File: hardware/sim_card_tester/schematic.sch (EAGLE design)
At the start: 146 parts, among them IC1 TPS6300, J2 MICRO_USB_B_HIROSE_ZX62R-B-5P, J3 CON_MICRO_SDDM3AT-SF-PEJM5, J4 NANO_SIM, J5 NANO_SIM, J6 TC2030-JLINK-NL, J7 NANO_SIM, J8 NANO_SIM, J9 U.FL-R-SMT, Q11 SI223DDS, Q3 MOSFET-NCHANNELSMD, Q4 MOSFET-NCHANNELSMD, Q5 MOSFET-NCHANNELSMD, U1 AB1815-T3, U10 SIP32510, U11 SIP32510, U14 SARA-U2, U15 MAX4734EUB+, U16 SARA-U2, U17 TXB0104RUT, U2 BGA725L6-ALT, U20 MAX4734EUB+, U21 MAX4734EUB+, U22 MAX4734EUB+, U3 FTDI234XD, U4 SAFFB1G56KB0F0A, U5 MAX8887EZK33+T, U6 MCP73831, U7 MAX-M8, U8 MAX67XXMAX6749MAX67XX, U9 NRF52840, X1 ABS07-32.768KHZ-7-T, X4 32MHz, X5 32.768kHz

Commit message: second pcb
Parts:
- removed C13: 33pF, passives:CAPACITOR0603_CAP
- removed C15: 100uF, passives:CAPACITOR0805_CAP
- removed C22, C24, C25, C26: 47pF, passives:CAPACITOR0402_CAP
- removed C49: 56pF, passives:CAPACITOR0402_CAP
- removed C50: 10nF, passives:CAPACITOR0402_CAP
- removed C51: 100nF, passives:CAPACITOR0402_CAP
- removed C52: 220uF, passives:CAPACITOR1210_CAP
- removed D10, D11, D8, D9: 14V, passives:DIODE_ZENER0402
- removed J9: U.FL-R-SMT, connector:U.FL-R-SMT
- removed Q11: SI223DDS, fets:SI223DDS
- removed Q4, Q5: MOSFET-NCHANNELSMD, fets:MOSFET-NCHANNELSMD
- removed R25: 10k, passives:RESISTOR0402_RES
- removed R36: 0, passives:RESISTOR0402_RES
- removed R40, R42: 100k, passives:RESISTOR0402_RES
- removed R45: 100, passives:RESISTOR0402_RES
- removed U14, U16: SARA-U2, ubloxLib:SARA-U2
- removed U17: TXB0104RUT, chips:TXB0104RUT
- added C11, C12, C16, C28: 47pF, passives:CAPACITOR0402_CAP
- added C17: 56pF, passives:CAPACITOR0402_CAP
- added C18: 100uF, passives:CAPACITOR0805_CAP
- added C19: 10nF, passives:CAPACITOR0402_CAP
- added C20: 220uF, passives:CAPACITOR1210_CAP
- added C21: 100nF, passives:CAPACITOR0402_CAP
- added C27: 33pF, passives:CAPACITOR0603_CAP
- added D3, D4, D6, D7: 14V, passives:DIODE_ZENER0402
- added J13: U.FL-R-SMT, connector:U.FL-R-SMT
- added Q2, Q6: MOSFET-NCHANNELSMD, fets:MOSFET-NCHANNELSMD
- added Q7: SI223DDS, fets:SI223DDS
- added R10: 10k, passives:RESISTOR0402_RES
- added R43, R46: 100k, passives:RESISTOR0402_RES
- added R47: 0, passives:RESISTOR0402_RES
- added R48: 100, passives:RESISTOR0402_RES
- added U12: UBLOX_SARA_G350, signpost:UBLOX_SARA_G350
- added U13: TXB0104RUT, chips:TXB0104RUT
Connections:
- removed net N$10: C13.2, R36.2
- removed net N$11: C13.1, U16A.ANT
- removed net N$50: J9.ANT, R36.1
- removed net N$52: Q4.D, Q5.D, U16A.DTR
- removed net N$54: Q4.S, U16A.!RESET
- removed net N$56: R42.2
- removed net N$57: Q5.S, U16A.PWR_ON
- removed net N$58: U16A.RTS, U17.A1
- removed net N$62: U16A.CTS, U17.A2
- removed net N$7: R25.1, U17.OE
- removed net N$80: Q11.G, R45.1
- removed net N$95: C22.2, C24.2, C25.2, C26.2, D10.ANODE, D11.ANODE, D8.ANODE, D9.ANODE
- removed net RXD: U16A.RXD, U17.A4
- removed net TXD: U16A.TXD, U17.A3
- removed net VBCKP: C15.1, R42.1, U14B.V_BCKP
- new net 3V3: R10.2, U13.VCC_B
- new net N$12: U12.RXD, U13.A4
- new net N$15: Q6.D, U12.RESET_N
- new net N$16: C18.1, R43.2, U12.V_BCKP
- new net N$18: Q2.D, R43.1, U12.PWR_ON
- new net N$25: U12.CTS, U13.A2
- new net N$53: U12.RTS, U13.A1
- new net N$63: C27.2, R47.1
- new net N$66: Q7.G, R48.1
- new net N$68: R10.1, U13.OE
- new net N$69: C27.1, U12.ANT
- new net N$70: J13.ANT, R47.2
- new net N$71: C11.2, C12.2, C16.2, C28.2, D3.ANODE, D4.ANODE, D6.ANODE, D7.ANODE
- new net N$9: U12.TXD, U13.A3
- net +3V3: no longer R25.2, U17.VCC_B
- net CLK_SIM: now also C28.1, D7.CATHODE, U12.SIM_CLK; no longer C26.1, D11.CATHODE, U14B.SIM_CLK
- net GND: now also C17.2, C18.2, C19.2, C20.2, C21.2, J13.P$2, Q2.S, Q6.S, R46.1, U12.DTR, U12.GND, U13.GND; no longer C15.2, C49.2, C50.2, C51.2, C52.2, J9.P$2, R40.1, U17.GND
- net GSM_3V8: now also Q7.S; no longer Q11.S
- net GSM_CTS: now also U13.B1; no longer U17.B1
- net GSM_GATED: now also C17.1, C19.1, C20.1, C21.1, Q7.D, U12.VCC; no longer C49.1, C50.1, C51.1, C52.1, Q11.D, U14B.VCC@3
- net GSM_LED: now also U12.GPIO1; no longer U16A.GPIO1
- net GSM_POWER: now also Q2.G; no longer Q5.G
- net GSM_POWER_GATE: now also R46.2, R48.2; no longer R40.2, R45.2
- net GSM_RST: now also Q6.G; no longer Q4.G
- net GSM_RTS: now also U13.B2; no longer U17.B2
- net GSM_RX: now also U13.B3; no longer U17.B3
- net GSM_TX: now also U13.B4; no longer U17.B4
- net IO_SIM: now also C11.1, D4.CATHODE, U12.SIM_IO; no longer C22.1, D9.CATHODE, U14B.SIM_IO
- net RST_SIM: now also C12.1, D6.CATHODE, U12.SIM_RST; no longer C24.1, D10.CATHODE, U14B.SIM_RST
- net VCC_SIM: now also C16.1, D3.CATHODE, U12.VSIM; no longer C25.1, D8.CATHODE, U14B.VSIM
- net V_GSM_INT: now also U12.V_INT, U13.VCC_A; no longer U14B.V_INT, U17.VCC_A
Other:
- note added: "UART lines for commands"

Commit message: fixed schematic and nrf routing
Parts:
- removed 20UF: (no value), Nordic_nRF:CAPACITOR_0201_L
- removed A4: ANT3216A063R2400A, chips:ANT3216A063R2400A
- removed C39: 1pF, passives:CAPACITOR0402_CAP
- removed L8: 3.9nH, passives:INDUCTOR0402
- removed LED1: BLUE, leds:LED0603
- removed Q3: MOSFET-NCHANNELSMD, fets:MOSFET-NCHANNELSMD
- removed R14: 10k, passives:RESISTOR0402_RES
- removed R20: 1k, passives:RESISTOR0402_RES
- removed R21: 100k, passives:RESISTOR0402_RES
- removed R47: 0, passives:RESISTOR0402_RES
- removed TP4: TPTP06SQ, testpad:TPTP06SQ
- added C50: 10uF, Nordic_nRF:CAPACITOR_0603_L
- added LED2: BLUE, leds:LED0603
- added Q1: MOSFET-NCHANNELSMD, fets:MOSFET-NCHANNELSMD
- added R11: 1k, BeagleBone_Black_Wireless:R-US_R0603
- added R12: 100k, BeagleBone_Black_Wireless:R-US_R0603
- 10UF: value (none) -> 10uF; device Nordic_nRF:CAPACITOR_0201_L -> Nordic_nRF:CAPACITOR_0603_L
- C11, C12, C14, C16, C17, C19, C2, C21, C23, C28, C3, C30, C31, C32, C33, C34, C35, C36, C37, C38, C4, C41, C42, C43, C44, C5, C55, C56, C58, C59, C6, C60, C61, C67, C68, C7, C8, C9: device passives:CAPACITOR0402_CAP -> Nordic_nRF:CAPACITOR_0603_L
- C18: device passives:CAPACITOR0805_CAP -> Nordic_nRF:CAPACITOR_0603_L
- C20: device passives:CAPACITOR1210_CAP -> Nordic_nRF:CAPACITOR_0603_L
- C27: device passives:CAPACITOR0603_CAP -> Nordic_nRF:CAPACITOR_0603_L
- C40: value 1pF -> 10uF; device passives:CAPACITOR0402_CAP -> Nordic_nRF:CAPACITOR_0603_L; DIGIKEY 490-3083-1-ND -> (none); MPN GJM1555C1H1R0CB01D -> (none)
- R1, R10, R13, R15, R16, R17, R18, R19, R2, R22, R27, R29, R3, R30, R31, R32, R33, R34, R35, R4, R41, R43, R46, R48, R5, R6, R7, R8, R9: device passives:RESISTOR0402_RES -> BeagleBone_Black_Wireless:R-US_R0603
- R23: device SparkFun-Resistors:100OHM-0603-1/4W-5% -> BeagleBone_Black_Wireless:R-US_R0603
- R24, R37, R38, R39: device SparkFun-Resistors:10KOHM-0603-1/10W-1% -> BeagleBone_Black_Wireless:R-US_R0603
- R26, R28: device SparkFun-Resistors:RESISTOR0402 -> BeagleBone_Black_Wireless:R-US_R0603
- U$5: device Nordic_nRF:CAPACITOR_0201_L -> Nordic_nRF:CAPACITOR_0603_L
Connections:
- removed net 0: J4.C5(GND), J5.C5(GND), J7.C5(GND), J8.C5(GND), U15.GND, U20.GND, U21.GND, U22.GND
- removed net 3V3: R10.2, U13.VCC_B
- removed net 5V: C67.1, FB2.P$2, J2.+5V, R41.1, R8.2, U6.VDD/1, U6.VDD/2
- removed net CONNECT: 10UF.1, C68.1, IC1G$1.VIN, R13.2, R23.2, U6.VBAT/3, U6.VBAT/4
- removed net GSM_3V8: Q7.S
- removed net N$30: IC1G$1.PGND
- removed net N$37: IC1G$1.GND
- removed net N$38: C39.1, L8.2, U9.ANT
- removed net N$42: A4.ANTENNA, C40.1, L8.1
- removed net N$44: LED1.CATHODE, Q3.D
- removed net N$49: LED1.ANODE, R20.1
- removed net N$51: 20UF.1, C58.1, IC1G$1.VOUT, R26.2, U5.!SHDN, U5.IN
- removed net N$63: C27.2, R47.1
- removed net RTC_CS: U9.P0.12
- removed net RTC_INT1: U9.P0.16
- new net N$14: LED2.CATHODE, Q1.D
- new net N$23: LED2.ANODE, R11.1
- net !EXTERNAL_RST: now also U9.P0.24
- net !RTC_CS: now also U9.P0.12
- net !RTC_INT1: now also U9.P0.16
- net +3V3: now also C10.1, C40.1, C50.1, C58.1, C67.1, IC1G$1.VOUT, Q7.S, R10.2, R15.1, R16.1, R26.2, R41.1, R8.2, U1.VCC, U13.VCC_B, U5.!SHDN, U5.IN, U6.VDD/1, U6.VDD/2
- net BAT: now also 10UF.1, C68.1, IC1G$1.VIN, R13.2, R23.2, U6.VBAT/3, U6.VBAT/4
- net BATIN: now also U9.P1.06; no longer U9.P0.30/AIN6
- net GND: now also C50.2, IC1G$1.GND, IC1G$1.PGND, J4.C5(GND), J5.C5(GND), J7.C5(GND), J8.C5(GND), Q1.S, R12.1, U15.GND, U20.GND, U21.GND, U22.GND; no longer 20UF.2, A4.GND, C39.2, Q3.S, R14.2, R21.1, TP4.TP
- net GSM_CTS: now also U9.P0.02/AIN0
- net GSM_GATED: now also R11.2; no longer R20.2
- net GSM_LED: now also Q1.G, R12.2; no longer Q3.G, R21.2
- net GSM_POWER: now also U9.P0.03/AIN1
- net GSM_RST: now also U9.P0.29/AIN5
- net GSM_RTS: now also U9.P0.28/AIN4
- net GSM_RX: now also U9.P0.30/AIN6
- net GSM_TX: now also U9.P0.31/AIN7
- net N$70: now also C27.2; no longer R47.2
- net VCC: now also FB2.P$2, J2.+5V; no longer C10.1, R15.1, R16.1, U1.VCC
- net WDI: no longer R14.1, U1.WDI
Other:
- note removed: "Edison Serial Header"
- note removed: "Must be a stable LDO for the DW1000."
- note removed: "Must not float. Could float if particle is sleeping - so pull down."
- moved on the sheet: R1, R10, R13, R15, R16, R17, R18, R19, R2, R22, R27, R29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

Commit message: fixed drc errors
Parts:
- C14: DESCRIPTION CAP CER 10UF 6.3V X5R 0402 -> (none); DIGIKEY 490-13211-1-ND -> 490-12538-1-ND; MANUFACTURER Murata Electronics North America -> Murata Electronics; MPN GRJ155R60J106ME11D -> GRM188R60J106KE47D
- C3: DESCRIPTION CAP CER 10000PF 16V X7R 0402 -> (none); DIGIKEY 490-1313-1-ND -> 490-7194-1-ND; MANUFACTURER Murata Electronics North America -> Murata Electronics; MPN GRM155R71C103KA01D -> GRM033R61E103KA12D
- C7: DESCRIPTION CAP CER 0.1UF 10V X5R 0402 -> (none); DIGIKEY 311-1336-1-ND -> 490-5405-1-ND; MANUFACTURER Yageo -> Murata Electronics; MPN CC0402KRX5R6BB104 -> GRM033R61A104ME15D
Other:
- note removed: "GPS and WiFi Radios"
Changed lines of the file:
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@@
 </part>
 <part name="C3" library="Nordic_nRF" library_urn="urn:adsk.eagle:library:169009" deviceset="CAPACITOR" device="_0603_L" package3d_urn="urn:adsk.eagle:package:2593727/1" value="10nF">
-<attribute name="DESCRIPTION" value="CAP CER 10000PF 16V X7R 0402"/>
-<attribute name="DIGIKEY" value="490-1313-1-ND"/>
-<attribute name="MANUFACTURER" value="Murata Electronics North America"/>
-<attribute name="MPN" value="GRM155R71C103KA01D"/>
+<attribute name="DIGIKEY" value="490-7194-1-ND"/>
+<attribute name="MANUFACTURER" value="Murata Electronics"/>
+<attribute name="MPN" value="GRM033R61E103KA12D"/>
 </part>
 <part name="C7" library="Nordic_nRF" library_urn="urn:adsk.eagle:library:169009" deviceset="CAPACITOR" device="_0603_L" package3d_urn="urn:adsk.eagle:package:2593727/1" value="0.1uF">
-<attribute name="DESCRIPTION" value="CAP CER 0.1UF 10V X5R 0402"/>
-<attribute name="DIGIKEY" value="311-1336-1-ND"/>
-<attribute name="MANUFACTURER" value="Yageo"/>
-<attribute name="MPN" value="CC0402KRX5R6BB104"/>
+<attribute name="DIGIKEY" value="490-5405-1-ND"/>
+<attribute name="MANUFACTURER" value="Murata Electronics"/>
+<attribute name="MPN" value="GRM033R61A104ME15D"/>
 </part>
 <part name="C14" library="Nordic_nRF" library_urn="urn:adsk.eagle:library:169009" deviceset="CAPACITOR" device="_0603_L" package3d_urn="urn:adsk.eagle:package:2593727/1" value="10uF">
-<attribute name="DESCRIPTION" value="CAP CER 10UF 6.3V X5R 0402"/>
-<attribute name="DIGIKEY" value="490-13211-1-ND"/>
-<attribute name="MANUFACTURER" value="Murata Electronics North America"/>
-<attribute name="MPN" value="GRJ155R60J106ME11D"/>
+<attribute name="DIGIKEY" value="490-12538-1-ND"/>
+<attribute name="MANUFACTURER" value="Murata Electronics"/>
+<attribute name="MPN" value="GRM188R60J106KE47D"/>
 </part>
 <part name="D5" library="leds" deviceset="LED" device="0603" value="BLUE">
@@
 <sheets>
 <sheet>
-<description>GPS and WiFi Radios</description>
+<description>GPS</description>
 <plain>
 <text x="-6.096" y="112.014" size="2.032" layer="98" align="top-right">https://www.u-blox.com/sites/default/files/MAX-8-M8-FW3_HardwareIntegrationManual_%28UBX-15030059%29.pdf</text>
-<text x="-35.56" y="17.78" size="5.08" layer="98" align="top-right">GPS and WiFi Radios</text>
 <text x="-121.92" y="21.59" size="5.08" layer="94" align="bottom-center">LNA</text>
-<text x="-93.98" y="99.06" size="3.048" layer="98" align="top-right">GPS</text>
+<text x="-99.06" y="101.6" size="3.048" layer="98" align="top-right">GPS</text>
 <text x="-77.47" y="34.29" size="5.08" layer="94" align="bottom-center">SAW</text>
 </plain>
@@
 </sheet>
 <sheet>
+<description>NRF</description>
 <plain>
 </plain>
@@
 </sheet>
 <sheet>
+<description>Power Suppy and Charging</description>
 <plain>
 <text x="35.56" y="73.66" size="3.81" layer="98" align="bottom-center">Power Supply and Charging</text>
@@
 </sheet>
 <sheet>
+<description>Sara U201</description>
 <plain>
 <text x="177.8" y="160.02" size="2.54" layer="97">Level Translator, GSM_INT = 1.8V</text>
@@
 </sheet>
 <sheet>
+<description>Sim Card Muxes</description>
 <plain>
 </plain>

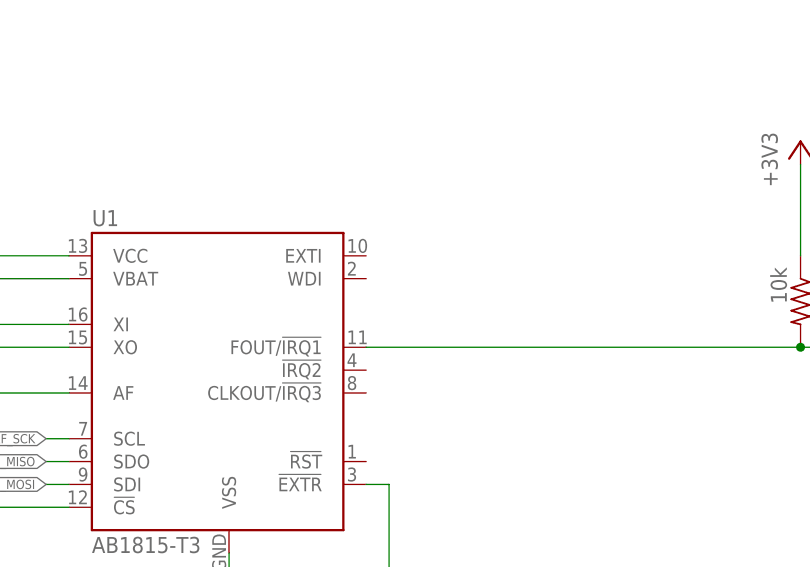
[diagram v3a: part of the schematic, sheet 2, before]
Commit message: add ground vias, label parts, clean up board
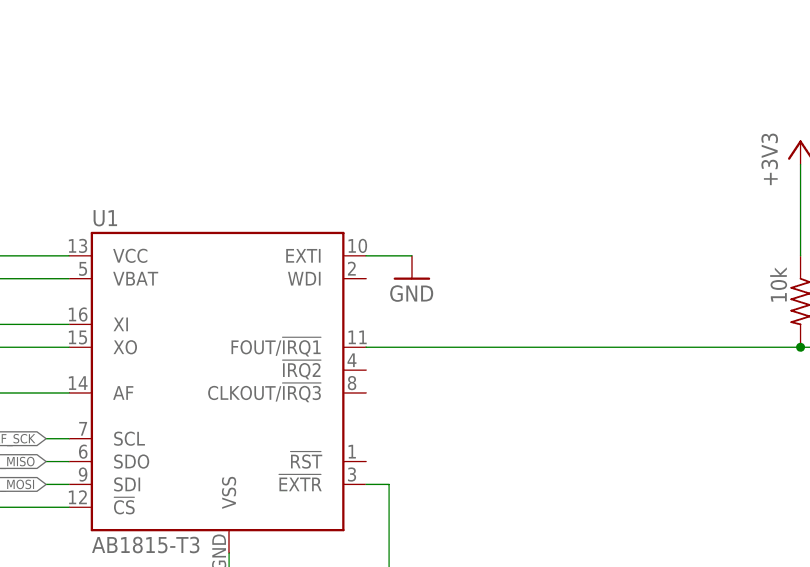
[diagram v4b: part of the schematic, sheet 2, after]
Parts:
- J6: value TC2030-JLINK-NL -> TC2030-JLINK-L; device connector:TC2030-JLINK-NL -> connector:TC2030-JLINK-L
- renumbered 10UF to C70
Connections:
- net GND: now also U1.EXTI
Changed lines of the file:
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@@
 <layers>
 <layer number="1" name="Top" color="4" fill="1" visible="no" active="no"/>
-<layer number="2" name="Route2" color="14" fill="1" visible="no" active="no"/>
-<layer number="3" name="Route3" color="4" fill="3" visible="no" active="no"/>
-<layer number="4" name="Route4" color="1" fill="4" visible="no" active="no"/>
-<layer number="5" name="Route5" color="4" fill="4" visible="no" active="no"/>
-<layer number="6" name="Route6" color="1" fill="8" visible="no" active="no"/>
-<layer number="7" name="Route7" color="4" fill="8" visible="no" active="no"/>
-<layer number="8" name="Route8" color="1" fill="2" visible="no" active="no"/>
-<layer number="9" name="Route9" color="4" fill="2" visible="no" active="no"/>
-<layer number="10" name="Route10" color="1" fill="7" visible="no" active="no"/>
-<layer number="11" name="Route11" color="4" fill="7" visible="no" active="no"/>
-<layer number="12" name="Route12" color="1" fill="5" visible="no" active="no"/>
-<layer number="13" name="Route13" color="4" fill="5" visible="no" active="no"/>
-<layer number="14" name="Route14" color="1" fill="6" visible="no" active="no"/>
-<layer number="15" name="Route15" color="11" fill="1" visible="no" active="no"/>
+<layer number="2" name="Route2" color="16" fill="1" visible="no" active="no"/>
+<layer number="3" name="Route3" color="17" fill="1" visible="no" active="no"/>
+<layer number="4" name="Route4" color="18" fill="1" visible="no" active="no"/>
+<layer number="5" name="Route5" color="19" fill="1" visible="no" active="no"/>
+<layer number="6" name="Route6" color="25" fill="1" visible="no" active="no"/>
+<layer number="7" name="Route7" color="26" fill="1" visible="no" active="no"/>
+<layer number="8" name="Route8" color="27" fill="1" visible="no" active="no"/>
+<layer number="9" name="Route9" color="28" fill="1" visible="no" active="no"/>
+<layer number="10" name="Route10" color="29" fill="1" visible="no" active="no"/>
+<layer number="11" name="Route11" color="30" fill="1" visible="no" active="no"/>
+<layer number="12" name="Route12" color="20" fill="1" visible="no" active="no"/>
+<layer number="13" name="Route13" color="21" fill="1" visible="no" active="no"/>
+<layer number="14" name="Route14" color="22" fill="1" visible="no" active="no"/>
+<layer number="15" name="Route15" color="23" fill="1" visible="no" active="no"/>
 <layer number="16" name="Bottom" color="1" fill="1" visible="no" active="no"/>
 <layer number="17" name="Pads" color="2" fill="1" visible="no" active="no"/>
 <layer number="18" name="Vias" color="2" fill="1" visible="no" active="no"/>
 <layer number="19" name="Unrouted" color="6" fill="1" visible="no" active="no"/>
-<layer number="20" name="Dimension" color="15" fill="1" visible="no" active="no"/>
+<layer number="20" name="Dimension" color="24" fill="1" visible="no" active="no"/>
 <layer number="21" name="tPlace" color="7" fill="1" visible="no" active="no"/>
 <layer number="22" name="bPlace" color="7" fill="1" visible="no" active="no"/>
@@
 <part name="IC1" library="texas" library_urn="urn:adsk.eagle:library:387" deviceset="TPS6300*" device=""/>
 <part name="L7" library="Nordic_nRF" library_urn="urn:adsk.eagle:library:169009" deviceset="INDUCTOR" device="_0201_L" package3d_urn="urn:adsk.eagle:package:2593725/1" value="2.2u"/>
-<part name="10UF" library="Nordic_nRF" library_urn="urn:adsk.eagle:library:169009" deviceset="CAPACITOR" device="_0603_L" package3d_urn="urn:adsk.eagle:package:2593727/1" value="10uF"/>
+<part name="C70" library="Nordic_nRF" library_urn="urn:adsk.eagle:library:169009" deviceset="CAPACITOR" device="_0603_L" package3d_urn="urn:adsk.eagle:package:2593727/1" value="10uF"/>
 <part name="R23" library="BeagleBone_Black_Wireless" library_urn="urn:adsk.eagle:library:6644236" deviceset="R-US_" device="R0603" package3d_urn="urn:adsk.eagle:package:8118505/1" value="100"/>
 <part name="U$5" library="Nordic_nRF" library_urn="urn:adsk.eagle:library:169009" deviceset="CAPACITOR" device="_0603_L" package3d_urn="urn:adsk.eagle:package:2593727/1" value=".1uF"/>
@@
 <part name="C33" library="Nordic_nRF" library_urn="urn:adsk.eagle:library:169009" deviceset="CAPACITOR" device="_0603_L" package3d_urn="urn:adsk.eagle:package:2593727/1" value="10nF"/>
 <part name="P+6" library="regulators" deviceset="+3V3" device="" value="3V8"/>
-<part name="J6" library="connector" deviceset="TC2030-JLINK" device="-NL"/>
+<part name="J6" library="connector" deviceset="TC2030-JLINK" device="-L" value="TC2030-JLINK-L"/>
 <part name="P+7" library="regulators" deviceset="+3V3" device=""/>
 <part name="GND19" library="supply1" library_urn="urn:adsk.eagle:library:371" deviceset="GND" device=""/>
@@
 <part name="P+1" library="regulators" deviceset="+3V3" device="" value="+5V"/>
 <part name="P+2" library="supply1" library_urn="urn:adsk.eagle:library:371" deviceset="VCC" device="" value="+5V"/>
+<part name="GND41" library="supply1" library_urn="urn:adsk.eagle:library:371" deviceset="GND" device=""/>
 </parts>
 <sheets>
@@
 <attribute name="REV" x="190.53175" y="-72.064878125" size="2.54" layer="94" font="vector" align="bottom-center"/>
 </instance>
+<instance part="GND41" gate="1" x="104.14" y="-20.32" smashed="yes">
+<attribute name="VALUE" x="101.6" y="-22.86" size="1.778" layer="96"/>
+</instance>
 </instances>
 <busses>
@@
 <junction x="83.82" y="-53.34"/>
 </segment>
+<segment>
+<pinref part="U1" gate="G$1" pin="EXTI"/>
+<pinref part="GND41" gate="1" pin="GND"/>
+<wire x1="99.06" y1="-17.78" x2="104.14" y2="-17.78" width="0.1524" layer="91"/>
+</segment>
 </net>
 <net name="BAT" class="0">
@@
 <attribute name="VALUE" x="71.12" y="6.35" size="1.778" layer="96" rot="R180"/>
 </instance>
-<instance part="10UF" gate="C$1" x="15.24" y="-15.24" smashed="yes">
+<instance part="C70" gate="C$1" x="15.24" y="-15.24" smashed="yes">
 <attribute name="NAME" x="16.764" y="-14.859" size="1.778" layer="95"/>
 <attribute name="VALUE" x="16.764" y="-19.939" size="1.778" layer="96"/>
@@
 </segment>
 <segment>
-<pinref part="10UF" gate="C$1" pin="2"/>
+<pinref part="C70" gate="C$1" pin="2"/>
 <pinref part="GND15" gate="1" pin="GND"/>
 <wire x1="15.24" y1="-20.32" x2="15.24" y2="-22.86" width="0.1524" layer="91"/>
@@
 <pinref part="R23" gate="G$1" pin="2"/>
 <junction x="33.02" y="-12.7"/>
-<pinref part="10UF" gate="C$1" pin="1"/>
+<pinref part="C70" gate="C$1" pin="1"/>
 <wire x1="15.24" y1="-12.7" x2="33.02" y2="-12.7" width="0.1524" layer="91"/>
 <wire x1="33.02" y1="-12.7" x2="53.34" y2="-12.7" width="0.1524" layer="91"/>
